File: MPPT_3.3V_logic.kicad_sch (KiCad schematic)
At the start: 11 parts, among them Q3 PMOS, Q6 PMOS, U5 TPS62177DQCR, U6 LTC4412xS6, U7 LTC4412xS6

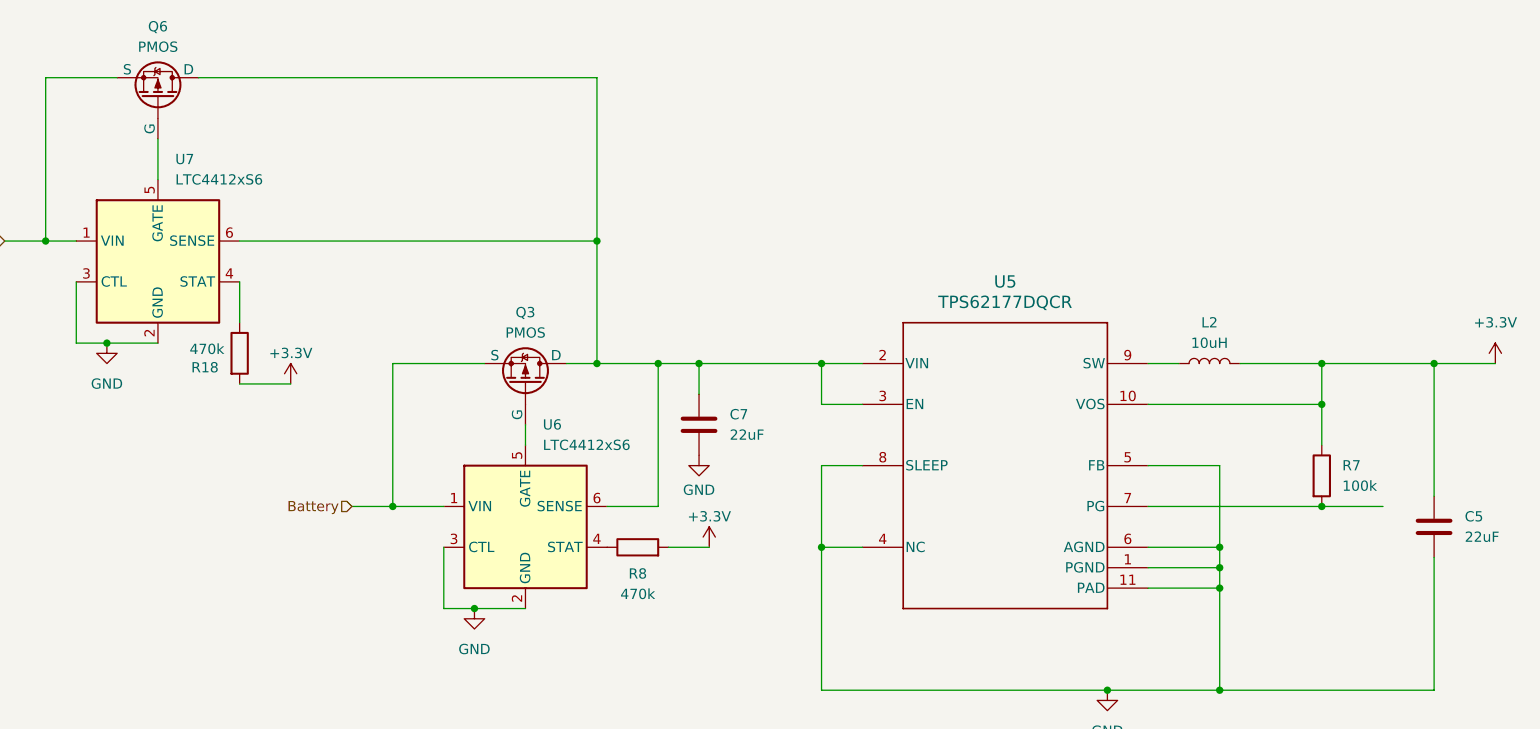
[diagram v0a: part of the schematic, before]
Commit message: Added cap to output of lines
based on LTSpice Simulation
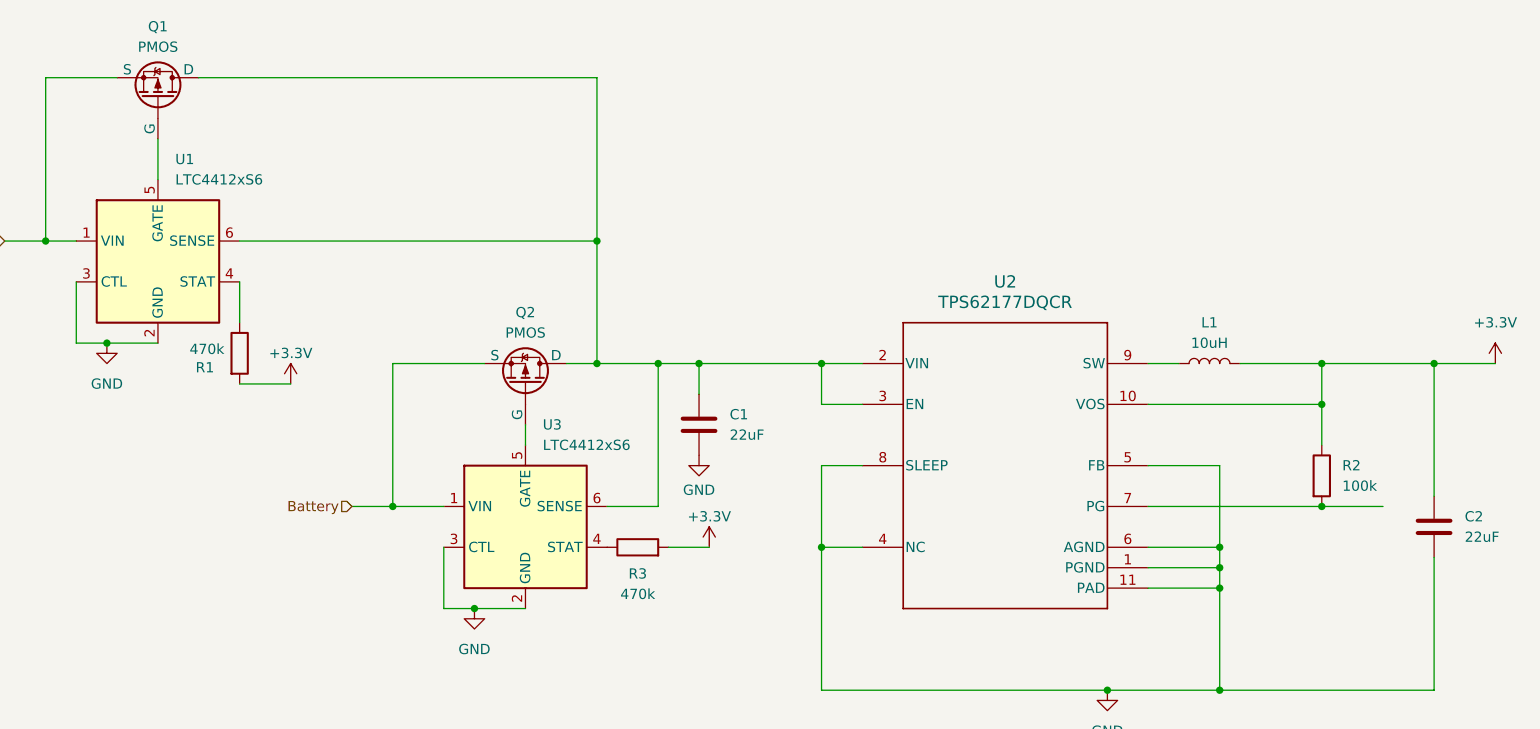
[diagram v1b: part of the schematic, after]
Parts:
- renumbered C7 to C1, C5 to C2, L2 to L1, Q6 to Q1, Q3 to Q2, R18 to R1, R7 to R2, R8 to R3, U7 to U1, U5 to U2, U6 to U3
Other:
- company: (none) -> QSET (Jaron Cyna)
- title: (none) -> EPS Board 3.3V Power with Bootstrap
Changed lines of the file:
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@@
 	(generator_version "9.0")
 	(paper "A4")
+	(title_block
+		(title "EPS Board 3.3V Power with Bootstrap")
+		(date "2026-03-17")
+		(rev "1.0")
+		(company "QSET (Jaron Cyna)")
+	)
 	(junction
 		(at 151.13 113.03)
@@
 		(on_board yes)
 		(dnp no)
-		(property "Reference" "#PWR041"
+		(property "Reference" "#PWR05"
 			(at 137.16 116.84 0)
 			(effects
@@
 			(project "EPS_mppt_board"
 				(path "/8f246f89-1ec7-4136-9977-839b50e116ed/1cb04f15-5cd4-4c9d-a391-62735eda9253"
-					(reference "#PWR041")
+					(reference "#PWR05")
 					(unit 1)
 				)
@@
 		(dnp no)
 		(fields_autoplaced yes)
-		(property "Reference" "C7"
+		(property "Reference" "C1"
 			(at 139.7 96.5199 0)
 			(effects
@@
 			(project ""
 				(path "/8f246f89-1ec7-4136-9977-839b50e116ed/1cb04f15-5cd4-4c9d-a391-62735eda9253"
-					(reference "C7")
+					(reference "C1")
 					(unit 1)
 				)
@@
 		(on_board yes)
 		(dnp no)
-		(property "Reference" "Q6"
+		(property "Reference" "Q1"
 			(at 68.58 48.26 90)
 			(effects
@@
 			(project "EPS_mppt_board"
 				(path "/8f246f89-1ec7-4136-9977-839b50e116ed/1cb04f15-5cd4-4c9d-a391-62735eda9253"
-					(reference "Q6")
+					(reference "Q1")
 					(unit 1)
 				)
@@
 		(dnp no)
 		(fields_autoplaced yes)
-		(property "Reference" "R7"
+		(property "Reference" "R2"
 			(at 215.9 102.8699 0)
 			(effects
@@
 			(project ""
 				(path "/8f246f89-1ec7-4136-9977-839b50e116ed/1cb04f15-5cd4-4c9d-a391-62735eda9253"
-					(reference "R7")
+					(reference "R2")
 					(unit 1)
 				)
@@
 		(on_board yes)
 		(dnp no)
-		(property "Reference" "Q3"
+		(property "Reference" "Q2"
 			(at 114.3 83.82 90)
 			(effects
@@
 			(project ""
 				(path "/8f246f89-1ec7-4136-9977-839b50e116ed/1cb04f15-5cd4-4c9d-a391-62735eda9253"
-					(reference "Q3")
+					(reference "Q2")
 					(unit 1)
 				)
@@
 		(dnp no)
 		(fields_autoplaced yes)
-		(property "Reference" "U6"
+		(property "Reference" "U3"
 			(at 116.4433 97.79 0)
 			(effects
@@
 			(project ""
 				(path "/8f246f89-1ec7-4136-9977-839b50e116ed/1cb04f15-5cd4-4c9d-a391-62735eda9253"
-					(reference "U6")
+					(reference "U3")
 					(unit 1)
 				)
@@
 		(on_board yes)
 		(dnp no)
-		(property "Reference" "#PWR039"
+		(property "Reference" "#PWR04"
 			(at 135.89 107.95 0)
 			(effects
@@
 			(project ""
 				(path "/8f246f89-1ec7-4136-9977-839b50e116ed/1cb04f15-5cd4-4c9d-a391-62735eda9253"
-					(reference "#PWR039")
+					(reference "#PWR04")
 					(unit 1)
 				)
@@
 		(dnp no)
 		(fields_autoplaced yes)
-		(property "Reference" "#PWR038"
+		(property "Reference" "#PWR06"
 			(at 107.95 127 0)
 			(effects
@@
 			(project ""
 				(path "/8f246f89-1ec7-4136-9977-839b50e116ed/1cb04f15-5cd4-4c9d-a391-62735eda9253"
-					(reference "#PWR038")
+					(reference "#PWR06")
 					(unit 1)
 				)
@@
 		(dnp no)
 		(fields_autoplaced yes)
-		(property "Reference" "U5"
+		(property "Reference" "U2"
 			(at 173.99 80.01 0)
 			(effects
@@
 			(project ""
 				(path "/8f246f89-1ec7-4136-9977-839b50e116ed/1cb04f15-5cd4-4c9d-a391-62735eda9253"
-					(reference "U5")
+					(reference "U2")
 					(unit 1)
 				)
@@
 		(on_board yes)
 		(dnp no)
-		(property "Reference" "R18"
+		(property "Reference" "R1"
 			(at 74.422 90.678 0)
 			(effects
@@
 			(project "EPS_mppt_board"
 				(path "/8f246f89-1ec7-4136-9977-839b50e116ed/1cb04f15-5cd4-4c9d-a391-62735eda9253"
-					(reference "R18")
+					(reference "R1")
 					(unit 1)
 				)
@@
 		(dnp no)
 		(fields_autoplaced yes)
-		(property "Reference" "#PWR037"
+		(property "Reference" "#PWR07"
 			(at 186.69 137.16 0)
 			(effects
@@
 			(project ""
 				(path "/8f246f89-1ec7-4136-9977-839b50e116ed/1cb04f15-5cd4-4c9d-a391-62735eda9253"
-					(reference "#PWR037")
+					(reference "#PWR07")
 					(unit 1)
 				)
@@
 		(dnp no)
 		(fields_autoplaced yes)
-		(property "Reference" "#PWR040"
+		(property "Reference" "#PWR02"
 			(at 234.95 93.98 0)
 			(effects
@@
 			(project ""
 				(path "/8f246f89-1ec7-4136-9977-839b50e116ed/1cb04f15-5cd4-4c9d-a391-62735eda9253"
-					(reference "#PWR040")
+					(reference "#PWR02")
 					(unit 1)
 				)
@@
 		(dnp no)
 		(fields_autoplaced yes)
-		(property "Reference" "U7"
+		(property "Reference" "U1"
 			(at 70.7233 64.77 0)
 			(effects
@@
 			(project "EPS_mppt_board"
 				(path "/8f246f89-1ec7-4136-9977-839b50e116ed/1cb04f15-5cd4-4c9d-a391-62735eda9253"
-					(reference "U7")
+					(reference "U1")
 					(unit 1)
 				)
@@
 		(dnp no)
 		(fields_autoplaced yes)
-		(property "Reference" "L2"
+		(property "Reference" "L1"
 			(at 199.39 85.09 90)
 			(effects
@@
 			(project ""
 				(path "/8f246f89-1ec7-4136-9977-839b50e116ed/1cb04f15-5cd4-4c9d-a391-62735eda9253"
-					(reference "L2")
+					(reference "L1")
 					(unit 1)
 				)
@@
 		(on_board yes)
 		(dnp no)
-		(property "Reference" "#PWR062"
+		(property "Reference" "#PWR03"
 			(at 85.09 96.52 0)
 			(effects
@@
 			(project "EPS_mppt_board"
 				(path "/8f246f89-1ec7-4136-9977-839b50e116ed/1cb04f15-5cd4-4c9d-a391-62735eda9253"
-					(reference "#PWR062")
+					(reference "#PWR03")
 					(unit 1)
 				)
@@
 		(on_board yes)
 		(dnp no)
-		(property "Reference" "R8"
+		(property "Reference" "R3"
 			(at 128.27 116.332 90)
 			(effects
@@
 			(project "EPS_mppt_board"
 				(path "/8f246f89-1ec7-4136-9977-839b50e116ed/1cb04f15-5cd4-4c9d-a391-62735eda9253"
-					(reference "R8")
+					(reference "R3")
 					(unit 1)
 				)
@@
 		(dnp no)
 		(fields_autoplaced yes)
-		(property "Reference" "C5"
+		(property "Reference" "C2"
 			(at 231.14 109.2199 0)
 			(effects
@@
 			(project ""
 				(path "/8f246f89-1ec7-4136-9977-839b50e116ed/1cb04f15-5cd4-4c9d-a391-62735eda9253"
-					(reference "C5")
+					(reference "C2")
 					(unit 1)
 				)
@@
 		(dnp no)
 		(fields_autoplaced yes)
-		(property "Reference" "#PWR061"
+		(property "Reference" "#PWR01"
 			(at 62.23 93.98 0)
 			(effects
@@
 			(project "EPS_mppt_board"
 				(path "/8f246f89-1ec7-4136-9977-839b50e116ed/1cb04f15-5cd4-4c9d-a391-62735eda9253"
-					(reference "#PWR061")
+					(reference "#PWR01")
 					(unit 1)
 				)

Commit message: Added footprints to caps
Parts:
- added C3: 22uF, Capacitor_SMD:C_0805_2012Metric, symbol Device:C
- C1: footprint (none) -> Capacitor_SMD:C_1210_3225Metric; MANUFACTURER (none) -> DigiKey; MANUFACTURER_PART_NUMBER (none) -> CL32B226KAJNFNE
- C2: footprint (none) -> Capacitor_SMD:C_0805_2012Metric; MANUFACTURER (none) -> DigiKey; MANUFACTURER_PART_NUMBER (none) -> GRM21BZ71A226ME15L
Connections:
- net +3.3V: now also C3.1
- net GND: now also C3.2
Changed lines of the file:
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@@
 		(company "QSET (Jaron Cyna)")
+	)
+	(text_box "Im using a smaller footprint here for these caps so I have two in parralell to combat the DC bias effect along with added redundancy"
+		(exclude_from_sim no)
+		(at 251.46 104.14 0)
+		(size 30.48 15.24)
+		(margins 0.9525 0.9525 0.9525 0.9525)
+		(stroke
+			(width 0)
+			(type solid)
+		)
+		(fill
+			(type color)
+			(color 158 218 255 1)
+		)
+		(effects
+			(font
+				(size 1.27 1.27)
+			)
+			(justify left top)
+		)
 	)
 	(junction
@@
 	)
 	(junction
+		(at 227.33 101.6)
+		(diameter 0)
+		(color 0 0 0 0)
+	)
+	(junction
+		(at 227.33 120.65)
+		(diameter 0)
+		(color 0 0 0 0)
+	)
+	(junction
 		(at 227.33 90.17)
 		(diameter 0)
@@
 	(wire
 		(pts
+			(xy 227.33 101.6) (xy 241.3 101.6)
+		)
+		(stroke
+			(width 0)
+			(type default)
+		)
+	)
+	(wire
+		(pts
 			(xy 68.58 62.23) (xy 68.58 67.31)
 		)
@@
 	(wire
 		(pts
+			(xy 241.3 101.6) (xy 241.3 106.68)
+		)
+		(stroke
+			(width 0)
+			(type default)
+		)
+	)
+	(wire
+		(pts
 			(xy 191.77 95.25) (xy 213.36 95.25)
 		)
@@
 	(wire
 		(pts
+			(xy 227.33 120.65) (xy 241.3 120.65)
+		)
+		(stroke
+			(width 0)
+			(type default)
+		)
+	)
+	(wire
+		(pts
 			(xy 124.46 107.95) (xy 130.81 107.95)
 		)
@@
 	(wire
 		(pts
-			(xy 227.33 90.17) (xy 227.33 106.68)
-		)
-		(stroke
-			(width 0)
-			(type default)
-		)
-	)
-	(wire
-		(pts
 			(xy 135.89 90.17) (xy 135.89 93.98)
 		)
@@
 	(wire
 		(pts
+			(xy 227.33 90.17) (xy 227.33 101.6)
+		)
+		(stroke
+			(width 0)
+			(type default)
+		)
+	)
+	(wire
+		(pts
 			(xy 200.66 130.81) (xy 227.33 130.81)
 		)
@@
 	(wire
 		(pts
+			(xy 241.3 120.65) (xy 241.3 114.3)
+		)
+		(stroke
+			(width 0)
+			(type default)
+		)
+	)
+	(wire
+		(pts
+			(xy 227.33 101.6) (xy 227.33 106.68)
+		)
+		(stroke
+			(width 0)
+			(type default)
+		)
+	)
+	(wire
+		(pts
 			(xy 78.74 74.93) (xy 123.19 74.93)
 		)
@@
 	(wire
 		(pts
+			(xy 227.33 120.65) (xy 227.33 130.81)
+		)
+		(stroke
+			(width 0)
+			(type default)
+		)
+	)
+	(wire
+		(pts
 			(xy 191.77 102.87) (xy 200.66 102.87)
 		)
@@
 	(wire
 		(pts
-			(xy 227.33 114.3) (xy 227.33 130.81)
+			(xy 227.33 114.3) (xy 227.33 120.65)
 		)
 		(stroke
@@
 			)
 		)
-		(property "Footprint" ""
+		(property "Footprint" "Capacitor_SMD:C_1210_3225Metric"
 			(at 136.8552 101.6 0)
 			(effects
@@
 			)
 		)
-		(property "Datasheet" "~"
+		(property "Datasheet" "https://mm.digikey.com/Volume0/opasdata/d220001/medias/docus/2113/CL32B226KAJNFNE_Spec.pdf"
 			(at 135.89 97.79 0)
 			(effects
@@
 				)
 				(hide yes)
+			)
+		)
+		(property "MANUFACTURER" "DigiKey"
+			(at 135.89 97.79 0)
+			(effects
+				(font
+					(size 1.27 1.27)
+				)
+			)
+		)
+		(property "MANUFACTURER_PART_NUMBER" "CL32B226KAJNFNE"
+			(at 135.89 97.79 0)
+			(effects
+				(font
+					(size 1.27 1.27)
+				)
 			)
 		)
@@
 	)
 	(symbol
+		(lib_id "Device:C")
+		(at 241.3 110.49 0)
+		(unit 1)
+		(exclude_from_sim no)
+		(in_bom yes)
+		(on_board yes)
+		(dnp no)
+		(fields_autoplaced yes)
+		(property "Reference" "C3"
+			(at 245.11 109.2199 0)
+			(effects
+				(font
+					(size 1.27 1.27)
+				)
+				(justify left)
+			)
+		)
+		(property "Value" "22uF"
+			(at 245.11 111.7599 0)
+			(effects
+				(font
+					(size 1.27 1.27)
+				)
+				(justify left)
+			)
+		)
+		(property "Footprint" "Capacitor_SMD:C_0805_2012Metric"
+			(at 242.2652 114.3 0)
+			(effects
+				(font
+					(size 1.27 1.27)
+				)
+				(hide yes)
+			)
+		)
+		(property "Datasheet" "https://search.murata.co.jp/Ceramy/image/img/A01X/G101/ENG/GRM21BZ71A226ME15-01.pdf"
+			(at 241.3 110.49 0)
+			(effects
+				(font
+					(size 1.27 1.27)
+				)
+				(hide yes)
+			)
+		)
+		(property "Description" "Unpolarized capacitor"
+			(at 241.3 110.49 0)
+			(effects
+				(font
+					(size 1.27 1.27)
+				)
+				(hide yes)
+			)
+		)
+		(property "MANUFACTURER" "DigiKey"
+			(at 241.3 110.49 0)
+			(effects
+				(font
+					(size 1.27 1.27)
+				)
+			)
+		)
+		(property "MANUFACTURER_PART_NUMBER" "GRM21BZ71A226ME15L"
+			(at 241.3 110.49 0)
+			(effects
+				(font
+					(size 1.27 1.27)
+				)
+			)
+		)
+		(pin "1"
+		)
+		(pin "2"
+		)
+		(instances
+			(project "EPS_mppt_board"
+				(path "/8f246f89-1ec7-4136-9977-839b50e116ed/1cb04f15-5cd4-4c9d-a391-62735eda9253"
+					(reference "C3")
+					(unit 1)
+				)
+			)
+		)
+	)
+	(symbol
 		(lib_id "power:GND")
 		(at 135.89 101.6 0)
@@
 			)
 		)
-		(property "Footprint" ""
+		(property "Footprint" "Capacitor_SMD:C_0805_2012Metric"
 			(at 228.2952 114.3 0)
 			(effects
@@
 			)
 		)
-		(property "Datasheet" "~"
+		(property "Datasheet" "https://search.murata.co.jp/Ceramy/image/img/A01X/G101/ENG/GRM21BZ71A226ME15-01.pdf"
 			(at 227.33 110.49 0)
 			(effects
@@
 			)
 		)
+		(property "MANUFACTURER" "DigiKey"
+			(at 227.33 110.49 0)
+			(effects
+				(font
+					(size 1.27 1.27)
+				)
+			)
+		)
+		(property "MANUFACTURER_PART_NUMBER" "GRM21BZ71A226ME15L"
+			(at 227.33 110.49 0)
+			(effects
+				(font
+					(size 1.27 1.27)
+				)
+			)
+		)

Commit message: edited 3V3 Logic to add Efuse and UVLO
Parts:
- added C5: 1nF, Capacitor_SMD:C_1210_3225Metric, symbol Device:C
- added C65: 100pF, Capacitor_SMD:C_1210_3225Metric, symbol Device:C
- added C66: 1uF, Capacitor_SMD:C_1210_3225Metric, symbol Device:C
- added C67: 22uF, Capacitor_SMD:C_1210_3225Metric, symbol Device:C
- added C68: 2.2nF, Capacitor_SMD:C_1210_3225Metric, symbol Device:C
- added C69: 100nF, Capacitor_SMD:C_1210_3225Metric, symbol Device:C
- added Q11: PMOS, symbol Simulation_SPICE:PMOS
- added R5: 665k, symbol Device:R
- added R58: 165k, symbol Device:R
- added R59: 499k, symbol Device:R
- added R60: 350k, symbol Device:R
- added R62: 3.3k, symbol Device:R
- added R63, R64: 100k, symbol Device:R
- added U16: TPS259470ARPWR, RPW0010A-MFG, symbol TPS259470:TPS259470ARPWR
- added U5: LTC2965HDD-PBF, IC's_Sat:DFN-8_DD_LIT, symbol LTC2965HDD#PBF:LTC2965HDD-PBF
- C1: value 22uF -> 100nF
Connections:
- net +3.3V: now also R63.1, R64.1
- net GND: now also C5.2, C65.2, C66.2, C67.2, C68.2, C69.2, R59.2, R62.2, U16.2 (OVLO), U16.8 (GND), U5.6 (RS), U5.7 (GND), U5.9 (GND); no longer U1.3 (CTL)
- net Solar_+X: now also Q11.1 (D), U5.1 (VIN); no longer Q1.3 (S)
- net at C1.1, Q1.1 (D), Q2.1 (D)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: now also R60.1, U16.5 (IN); no longer U2.2 (VIN), U2.3 (EN)
- net at Q1.2 (G), U1.5 (GATE): now also Q11.2 (G)
- new net: R58.2, R59.1, U5.4 (INL)
- new net: Q1.3 (S), Q11.3 (S)
- new net: R60.2, U16.1 (EN_UVLO)
- new net: C66.1, C67.1, C69.1, U16.6 (OUT), U2.2 (VIN), U2.3 (EN)
- new net: R63.2, U16.3 (AUXOFF)
- new net: C68.1, U16.10 (ITIMER)
- new net: R64.2, U16.4 (!FLT)
- new net: C65.1, U16.7 (dVdt)
- new net: R62.1, U16.9 (ILM)
- new net: C5.1, R5.1, U5.2 (REF), U5.5 (PS)
- new net: R5.2, R58.1, U5.3 (INH)
- new net Cont: U1.3 (CTL), U5.8 (OUT)
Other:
- note added: "Buck Converter For On-Board 3.3V Logic"
- note added: "E-Fuse"
- note added: "Ideal Diode ORing Circuit"
- note added: "UVLO (for solar input)"
- moved on the sheet: C1, C2, C3, L1, Q1, Q2, R1, R2, R3, U1, U2, U3
